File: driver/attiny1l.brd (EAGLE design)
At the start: 35.8 x 20 mm, 9 parts, among them IC1 ATTiny85, IC4 LB1973M, J1 AVR_SPI_PRG_6NS

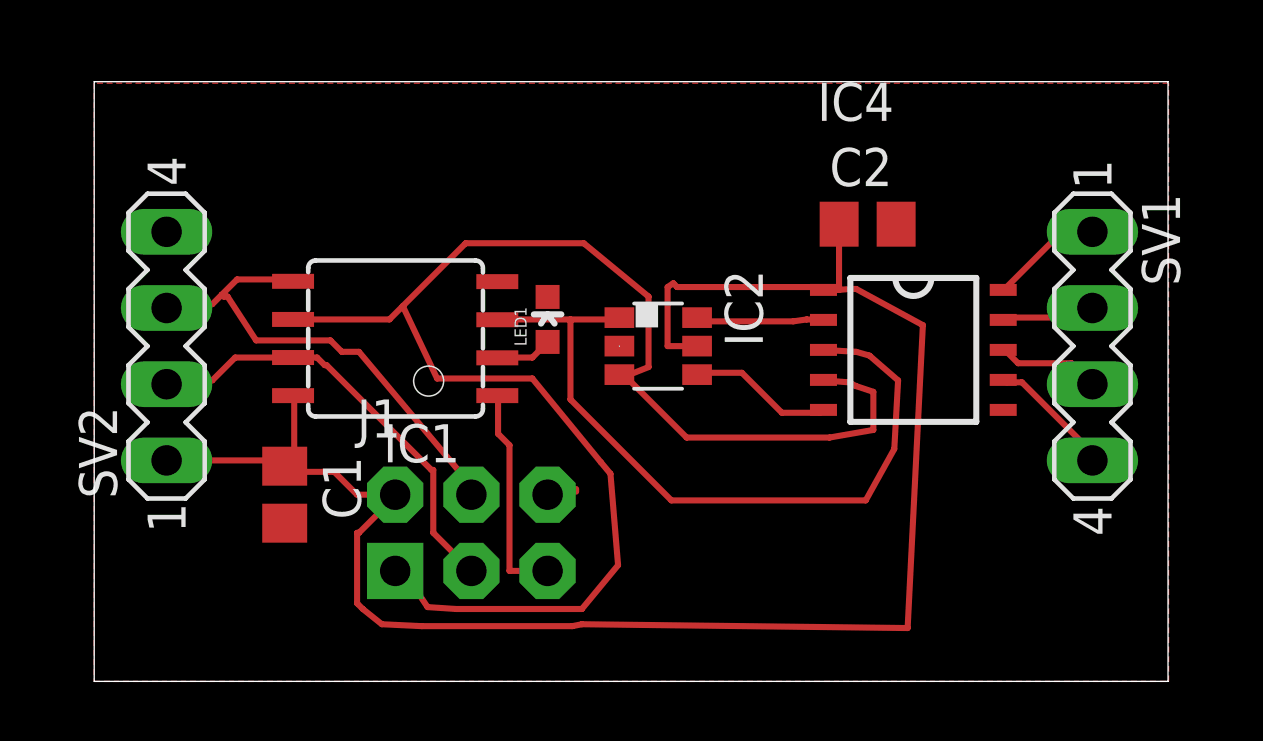
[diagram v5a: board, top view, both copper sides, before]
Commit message: otoh this way I can sample our input voltage when not driving the led...
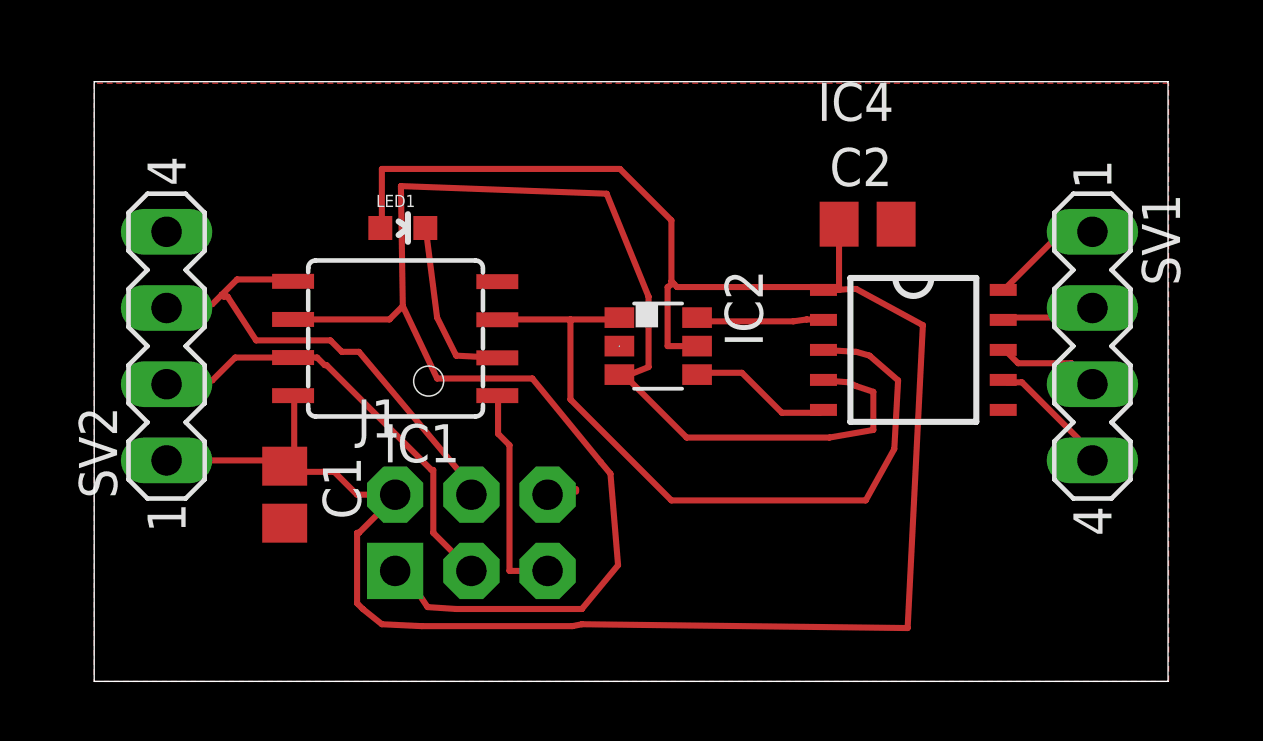
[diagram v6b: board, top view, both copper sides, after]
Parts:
- moved LED1 5.71 mm to (10.3, 15.1), turned to 270 degrees
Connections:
- net +5V: now also LED1.A
- net GND: no longer LED1.C
- net N$3: now also LED1.C; no longer LED1.A
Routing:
- net +5V: track 58.3 -> 72.8 mm
- net IN1/MISO: track 50.9 -> 55.8 mm
- net N$3: track 1.90 -> 5.82 mm
- net GND: track 0.97 -> 2.58 mm
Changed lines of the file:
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@@
 <element name="C1" library="rcl" package="C0805" value="" x="6.35" y="6.223" rot="R270"/>
 <element name="C2" library="rcl" package="C0805" value="" x="25.781" y="15.24"/>
-<element name="LED1" library="SparkFun-LED" package="LED-0603" value="" x="15.113" y="12.065"/>
+<element name="LED1" library="SparkFun-LED" package="LED-0603" value="" x="10.287" y="15.113" rot="R270"/>
 </elements>
 <signals>
@@
 <wire x1="17.526" y1="10.2235" x2="17.506" y2="10.226" width="0.2032" layer="1"/>
 <wire x1="9.8425" y1="12.065" x2="6.629" y2="12.065" width="0.2032" layer="1"/>
-<wire x1="12.3825" y1="14.605" x2="10.287" y2="12.5095" width="0.2032" layer="1"/>
+<wire x1="10.2235" y1="16.51" x2="10.287" y2="12.5095" width="0.2032" layer="1"/>
 <wire x1="10.287" y1="12.5095" x2="9.8425" y2="12.065" width="0.2032" layer="1"/>
-<wire x1="16.3195" y1="14.605" x2="12.3825" y2="14.605" width="0.2032" layer="1"/>
-<wire x1="18.4785" y1="12.827" x2="16.3195" y2="14.605" width="0.2032" layer="1"/>
+<wire x1="17.0815" y1="16.256" x2="10.2235" y2="16.51" width="0.2032" layer="1"/>
+<wire x1="18.4785" y1="12.827" x2="17.0815" y2="16.256" width="0.2032" layer="1"/>
 <wire x1="18.4785" y1="10.4775" x2="18.4785" y2="12.827" width="0.2032" layer="1"/>
 <wire x1="17.8435" y1="10.2235" x2="18.4785" y2="10.4775" width="0.2032" layer="1"/>
@@
 <contactref element="IC4" pad="6"/>
 <contactref element="IC2" pad="2"/>
-<contactref element="C1" pad="2"/>
 <contactref element="C2" pad="2"/>
 <wire x1="15.6845" y1="6.4135" x2="15.6845" y2="6.32459375" width="0.2032" layer="1"/>
 <wire x1="15.6845" y1="6.4135" x2="15.113" y2="6.223" width="0.2032" layer="1"/>
 <wire x1="16.0655" y1="6.4135" x2="16.0655" y2="6.32459375" width="0.2032" layer="1"/>
-<contactref element="LED1" pad="C"/>
 <wire x1="30.353" y1="9.0805" x2="30.301" y2="9.049" width="0.2032" layer="1"/>
 <wire x1="30.353" y1="9.0805" x2="30.30103125" y2="9.0490125" width="0.2032" layer="1"/>
 <wire x1="30.2895" y1="9.0805" x2="30.301" y2="9.049" width="0.2032" layer="1"/>
 <wire x1="30.2895" y1="9.0805" x2="30.30103125" y2="9.0490125" width="0.2032" layer="1"/>
-<wire x1="17.506" y1="11.176" x2="16.0655" y2="6.4135" width="0" layer="19" extent="1-1"/>
-<wire x1="15.113" y1="12.815" x2="17.506" y2="11.176" width="0" layer="19" extent="1-1"/>
-<wire x1="6.35" y1="5.273" x2="15.113" y2="6.223" width="0" layer="19" extent="1-1"/>
+<contactref element="C1" pad="2"/>
+<wire x1="15.24" y1="7.0485" x2="15.113" y2="6.223" width="0.2032" layer="1"/>
+<wire x1="15.24" y1="7.0485" x2="15.21459375" y2="7.0485" width="0.2032" layer="1"/>
+<wire x1="15.3035" y1="6.858" x2="15.113" y2="6.223" width="0.2032" layer="1"/>
+<wire x1="15.3035" y1="6.858" x2="15.21459375" y2="6.858" width="0.2032" layer="1"/>
+<wire x1="15.113" y1="6.223" x2="6.35" y2="5.273" width="0" layer="19" extent="1-1"/>
+<wire x1="17.506" y1="11.176" x2="15.24" y2="7.0485" width="0" layer="19" extent="1-1"/>
+<wire x1="13.437" y1="13.325" x2="17.506" y2="11.176" width="0" layer="19" extent="1-1"/>
 </signal>
 <signal name="+5V">
@@
 <wire x1="19.431" y1="13.1445" x2="19.304" y2="13.2715" width="0.2032" layer="1"/>
 <wire x1="24.1935" y1="13.1445" x2="24.309" y2="13.049" width="0.2032" layer="1"/>
+<contactref element="LED1" pad="A"/>
+<wire x1="9.5885" y1="17.0815" x2="9.5885" y2="15.113" width="0.2032" layer="1"/>
+<wire x1="17.526" y1="17.0815" x2="9.5885" y2="17.0815" width="0.2032" layer="1"/>
+<wire x1="19.2405" y1="15.367" x2="17.526" y2="17.0815" width="0.2032" layer="1"/>
+<wire x1="19.2405" y1="13.335" x2="19.2405" y2="15.367" width="0.2032" layer="1"/>
+<wire x1="9.5885" y1="15.113" x2="9.537" y2="15.113" width="0.2032" layer="1"/>
+<wire x1="19.2405" y1="13.335" x2="19.304" y2="13.2715" width="0.2032" layer="1"/>
 </signal>
 <signal name="SDA/MOSI">
@@
 </signal>
 <signal name="N$3">
+<contactref element="LED1" pad="C"/>
 <contactref element="IC1" pad="2"/>
-<contactref element="LED1" pad="A"/>
-<wire x1="14.605" y1="10.795" x2="15.113" y2="11.303" width="0.2032" layer="1"/>
-<wire x1="13.462" y1="10.795" x2="14.605" y2="10.795" width="0.2032" layer="1"/>
-<wire x1="15.113" y1="11.303" x2="15.113" y2="11.315" width="0.2032" layer="1"/>
-<wire x1="13.462" y1="10.795" x2="13.437" y2="10.785" width="0.2032" layer="1"/>
+<wire x1="11.43" y1="12.1285" x2="11.049" y2="15.113" width="0.2032" layer="1"/>
+<wire x1="12.065" y1="10.8585" x2="11.43" y2="12.1285" width="0.2032" layer="1"/>
+<wire x1="13.2715" y1="10.795" x2="12.065" y2="10.8585" width="0.2032" layer="1"/>
+<wire x1="13.3985" y1="10.795" x2="13.2715" y2="10.795" width="0.2032" layer="1"/>
+<wire x1="11.049" y1="15.113" x2="11.037" y2="15.113" width="0.2032" layer="1"/>
+<wire x1="13.3985" y1="10.795" x2="13.437" y2="10.785" width="0.2032" layer="1"/>
 </signal>
 </signals>
